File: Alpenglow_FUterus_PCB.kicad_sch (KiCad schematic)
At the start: 8 parts

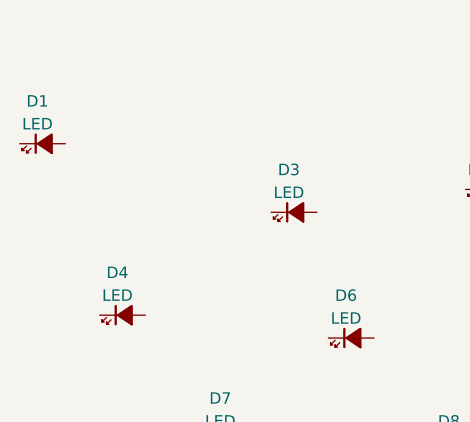
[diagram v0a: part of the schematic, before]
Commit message: Added easyeda library and LED side mount pattern, updated PCB, aligned uterus copper & mask
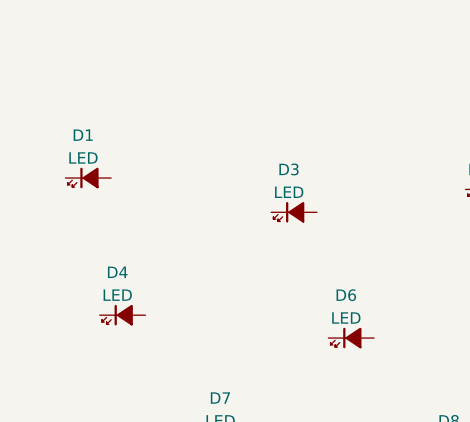
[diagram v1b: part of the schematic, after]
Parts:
- D1, D2, D3, D4, D5, D6, D7, D8: footprint Alpenglow:LED_1206+ -> easyeda2kicad:LED-SMD_L3.8-W1.0-R-RD_RED
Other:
- moved on the sheet: D1

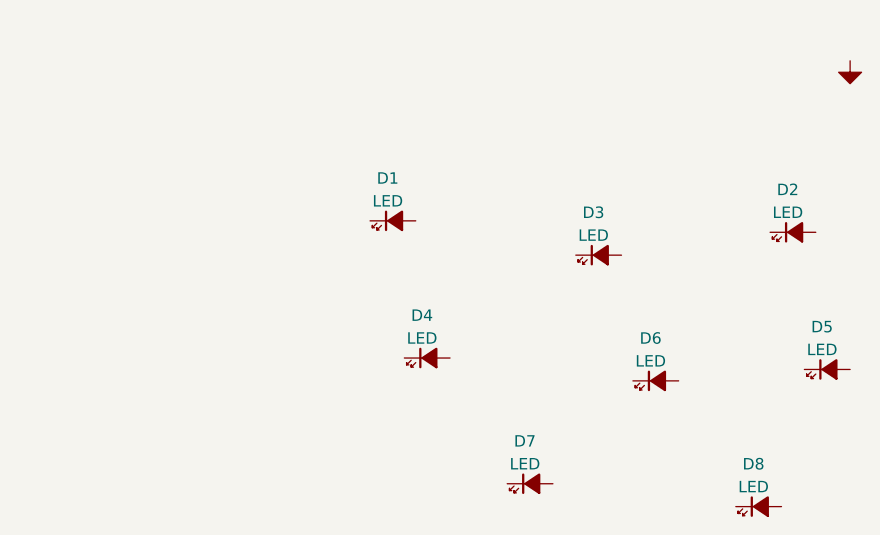
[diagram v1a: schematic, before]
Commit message: still a WIP, working on main component placement, considering processor vs self-blinking LEDs
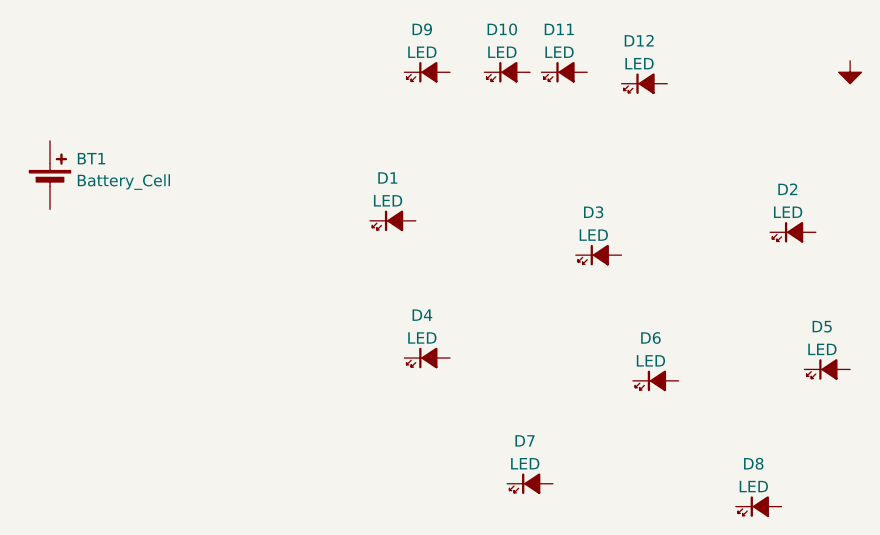
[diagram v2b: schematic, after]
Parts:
- added BT1: Battery_Cell, Alpenglow:BatteryHolder_CR2032_SMT, symbol Device:Battery_Cell
- added D10, D11, D12, D9: LED, easyeda2kicad:LED-SMD_L3.8-W1.0-R-RD_RED, symbol Alpenglow:LED

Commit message: picked it back up and started changes for through-hole kit
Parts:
- removed D10, D11, D12, D4, D5, D6, D7, D8, D9: LED, easyeda2kicad:LED-SMD_L3.8-W1.0-R-RD_RED, symbol Alpenglow:LED
- added SW1: SW_SLIDE, Alpenglow:SW_SPDT_SLIDE_THRU_RTA, symbol Alpenglow:SW_SLIDE
- D1, D2, D3: value LED -> RED; footprint easyeda2kicad:LED-SMD_L3.8-W1.0-R-RD_RED -> LED_THT:LED_D5.0mm_Horizontal_O3.81mm_Z3.0mm
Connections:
- net GND: now also BT1.2 (-), D1.1 (K), D2.1 (K), D3.1 (K)
- net LED+: now reaches D2.2 (A)
- net LED+: now also D1.2 (A), D3.2 (A), SW1.3
- net BATT+: now reaches BT1.1 (+)
- net BATT+: now also SW1.2
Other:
- moved on the sheet: BT1, D1, D2, D3

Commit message: artwork progress, still needs cleanup
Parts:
- removed SW1: SW_SLIDE, Alpenglow:SW_SPDT_SLIDE_THRU_RTA, symbol Alpenglow:SW_SLIDE
- added R1: RES, Resistor_THT:R_Axial_DIN0207_L6.3mm_D2.5mm_P10.16mm_Horizontal, symbol Alpenglow:RES
- added SW1: SW_SLIDE, Alpenglow:SW_SPDT_SLIDE_THRU_RTA, symbol Alpenglow:SW_SLIDE_BIG_NOMNT
- BT1: value Battery_Cell -> CR2032; footprint Alpenglow:BatteryHolder_CR2032_SMT -> Alpenglow:CR2032_Holder_Clip_Through_Hole-BS-03-A1AJ001
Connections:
- net BATT+: now also SW1.2
- net LED+: now also R1.2
- new net: R1.1, SW1.3
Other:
- moved on the sheet: BT1, D1, D2, D3
